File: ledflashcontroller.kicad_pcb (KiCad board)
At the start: 2 copper layers, 100 x 100 mm, 68 parts, among them J1 Conn_02x08_Odd_Even, J2 CONN_01X02, J3 CONN_01X02, K1 LDD-1000H, K2 LDD-1000H, P1 V_IN, P10 BNC, P11 BNC, P12 BNC, P2 I2C_HEADER, P3 GPIO_HEADER, P4 V_DIM1, P5 V_DIM2, P6 V_OUT, P7 BNC, P8 BNC, P9 BNC, Q1 IRLML6244, Q2 IRFB3256, U1 Teensy3.6, U10 DMC2700, U2 ISO1540, U3 DMC2700, U4 DMC2700, U5 ISO1540, U6 DMC2700, U7 DMC2700, U8 ISO1540, U9 DMC2700

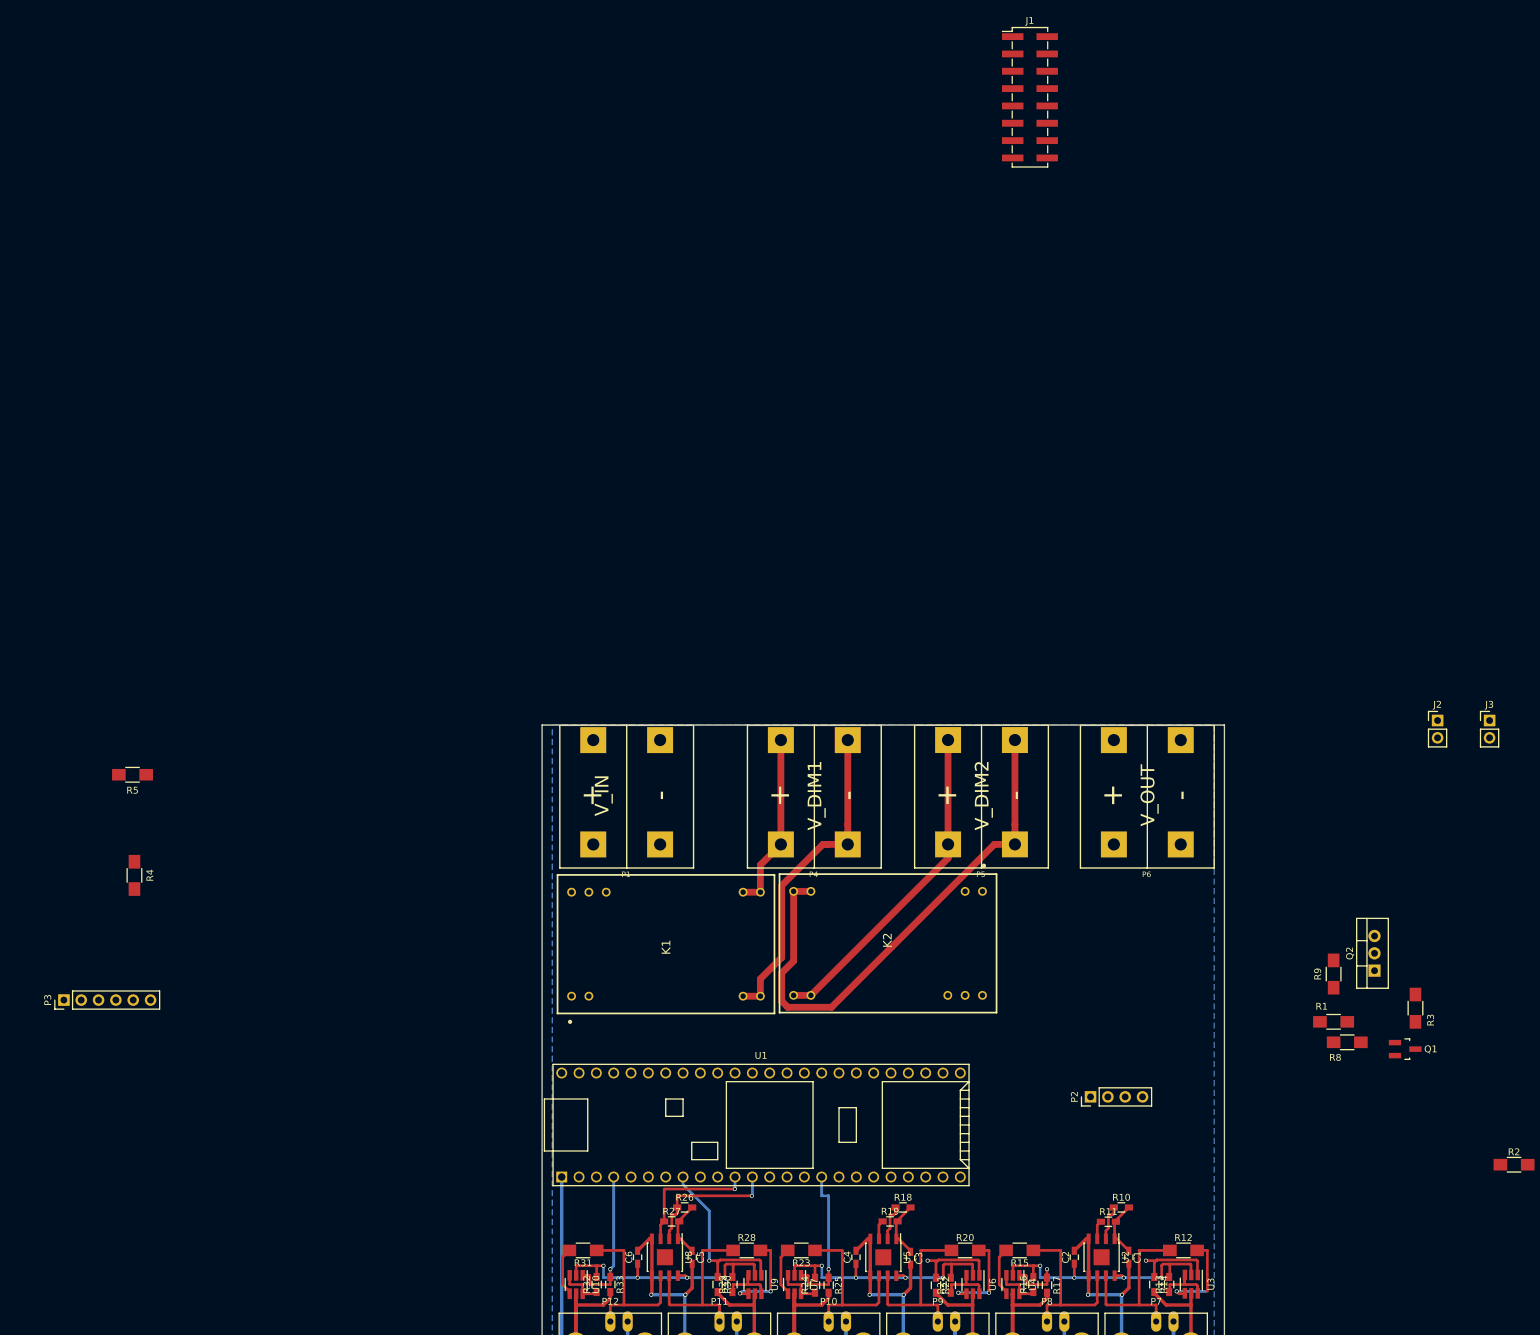
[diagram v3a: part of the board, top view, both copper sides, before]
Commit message: Fixed bugs (wires to close to pads)
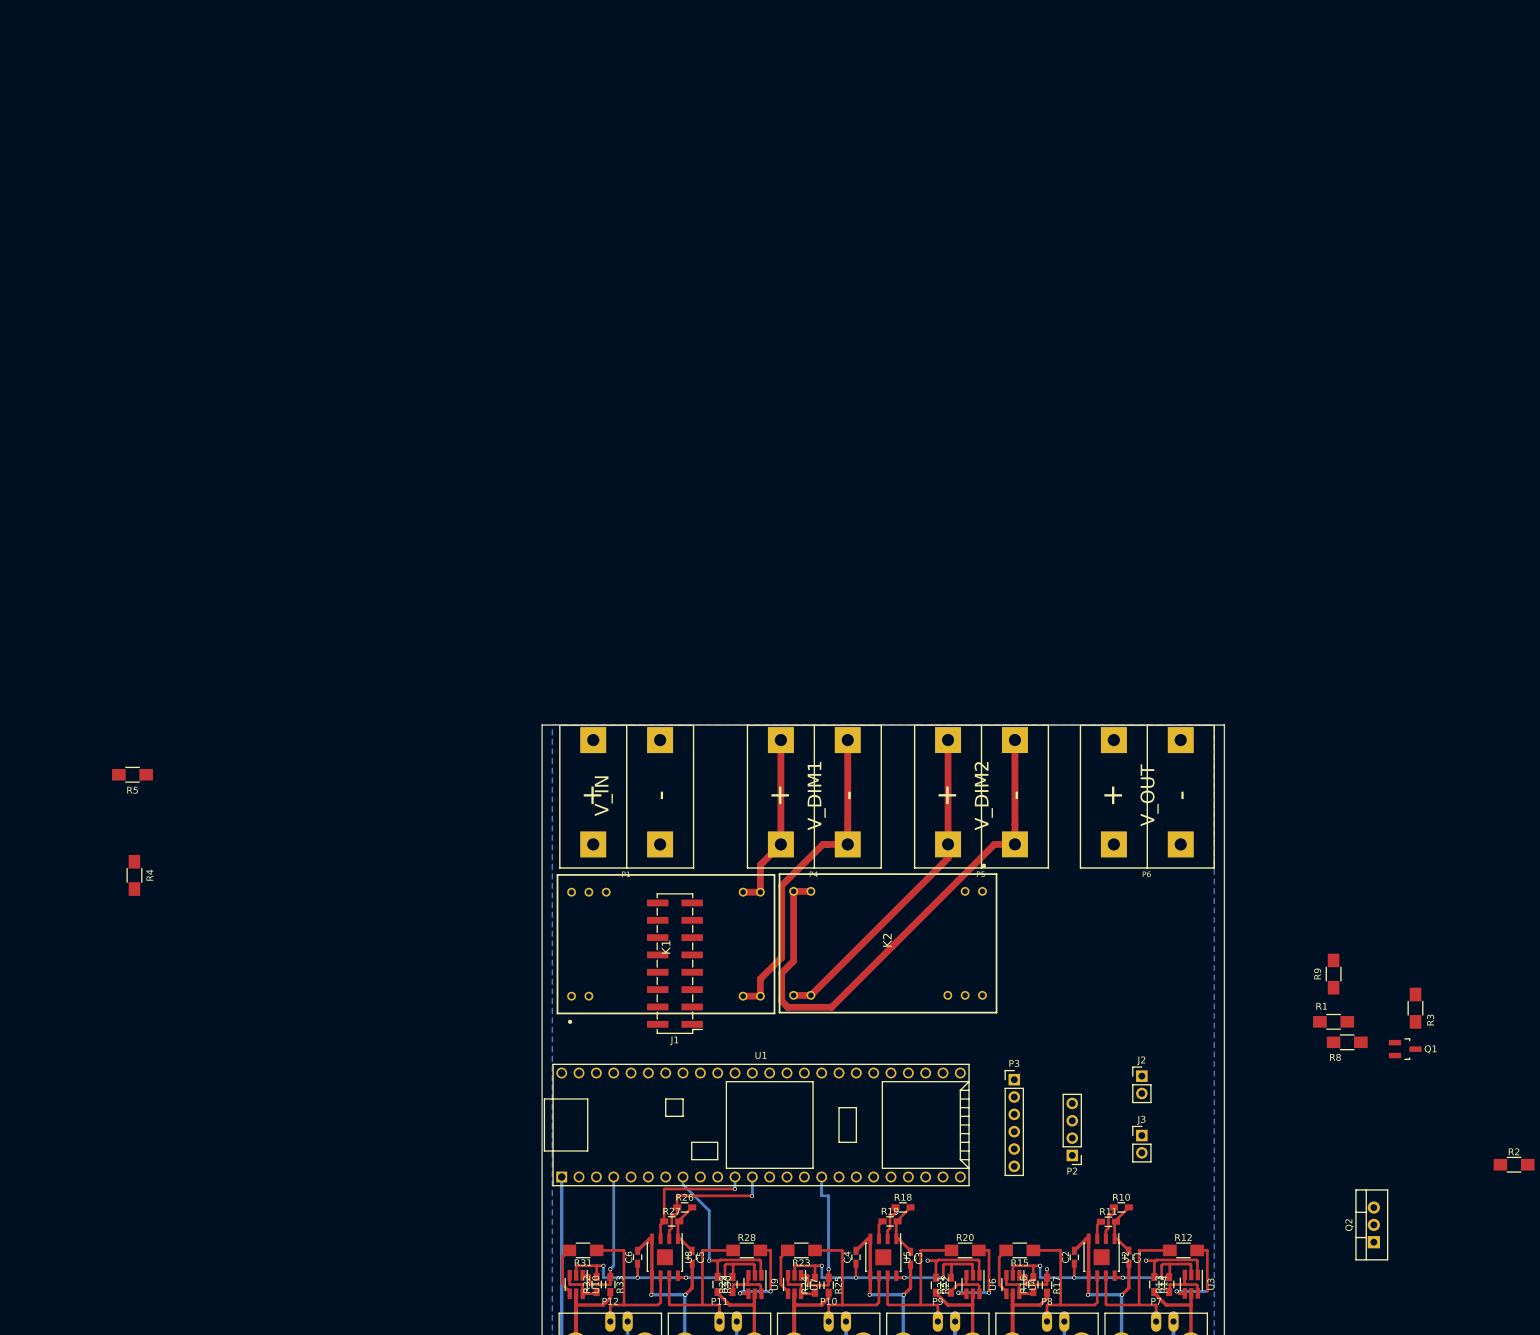
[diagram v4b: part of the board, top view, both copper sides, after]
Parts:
- moved P3 139.8 mm to (99.2, 82.0), turned to 0 degrees
- moved J1 137.2 mm to (49.5, 65.0), turned to 180 degrees
- moved J3 79.3 mm to (117.9, 90.2)
- moved J2 67.8 mm to (117.9, 81.5)
- moved Q2 39.8 mm to (151.9, 105.8)
- moved P2 8.99 mm to (107.7, 93.1), turned to 180 degrees

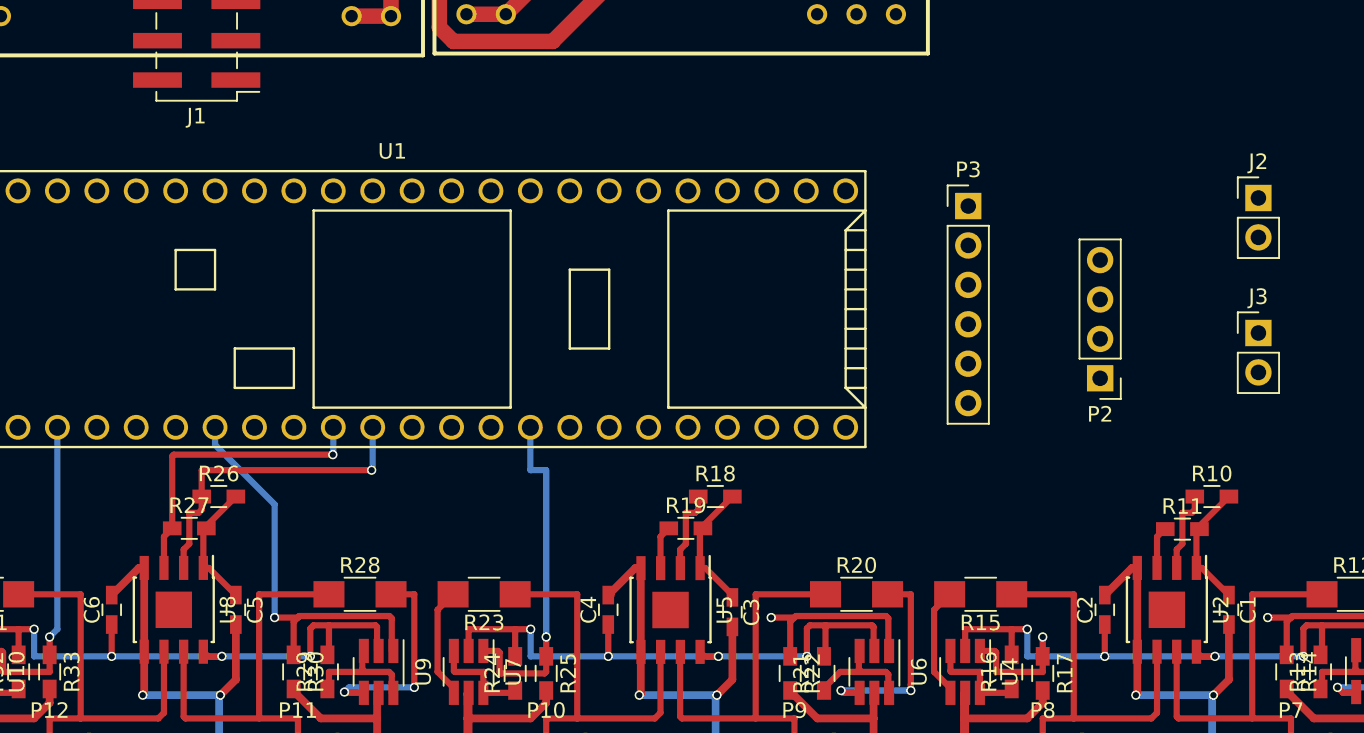
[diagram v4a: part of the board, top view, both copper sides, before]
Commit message: Connected circuits to Teensy
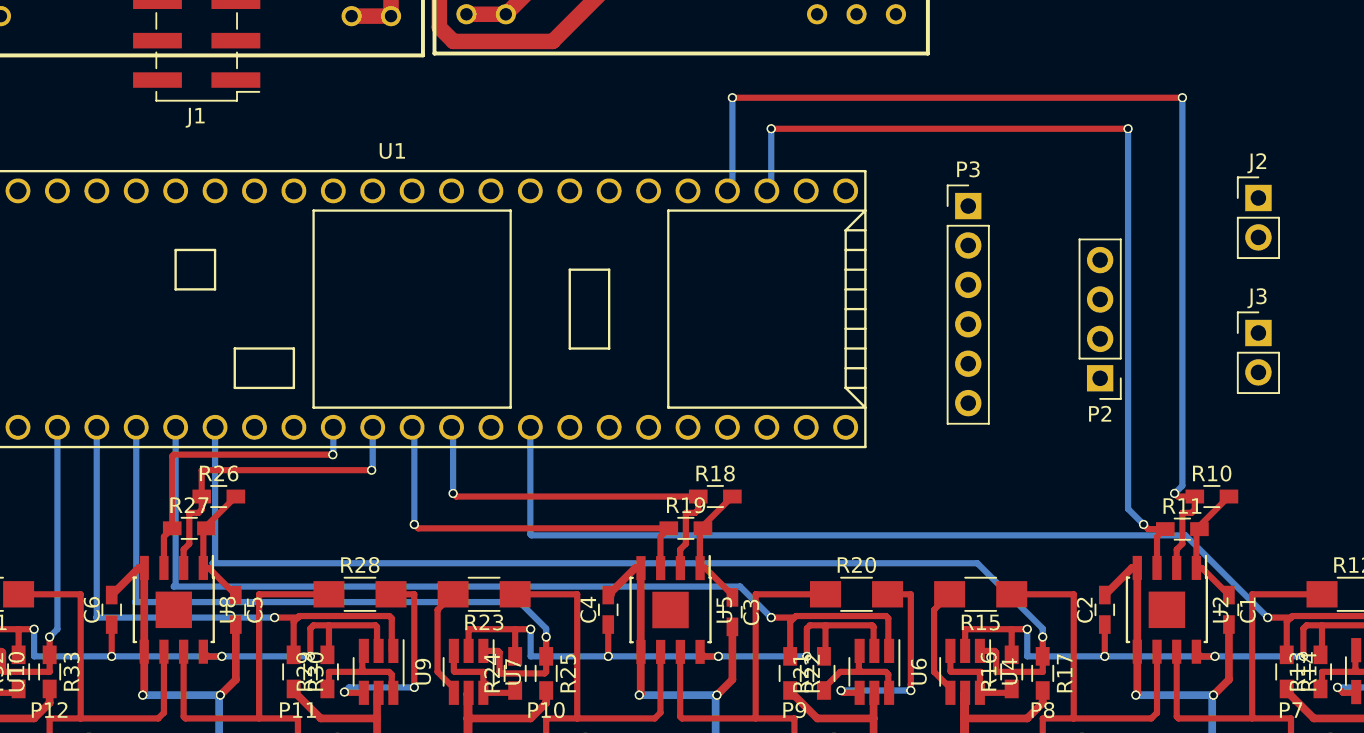
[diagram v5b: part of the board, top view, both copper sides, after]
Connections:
- R10 pad 1: /TRIG_IO0 -> /TRIG_IO9
- R11 pad 1: /TRIG_IO1 -> /TRIG_IO8
- R18 pad 1: /TRIG_IO2 -> /TRIG_IO7
- R19 pad 1: /TRIG_IO5 -> /TRIG_IO6
- U1 pad 16: /TRIG_PU5 -> /TRIG_PU0
- U1 pad 40: /TRIG_IO5 -> (no net)
- U1 pad 42: /TRIG_IO0 -> (no net)
- U1 pad 49: /TRIG_IO1 -> (no net)
- U1 pad 5: /TRIG_PU1 -> /TRIG_PU4
- U1 pad 50: /TRIG_IO2 -> (no net)
- U1 pad 6: /TRIG_PU2 -> /TRIG_PU5
- U1 pad 7: /TRIG_PU0 -> /TRIG_PU2
- U1 pad 8: /TRIG_PU4 -> /TRIG_PU1
- U2 pad 2: /TRIG_IO0 -> /TRIG_IO9
- U2 pad 3: /TRIG_IO1 -> /TRIG_IO8
- U5 pad 2: /TRIG_IO2 -> /TRIG_IO7
- U5 pad 3: /TRIG_IO5 -> /TRIG_IO6
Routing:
- net /TRIG_IO9: track 0.00 -> 67.7 mm, vias 0 -> 3
- net /TRIG_PU1: track 7.59 -> 72.2 mm
- net /TRIG_IO8: track 0.00 -> 57.3 mm, vias 0 -> 3
- net /TRIG_PU0: track 12.4 -> 69.0 mm
- net /TRIG_PU2: track 12.4 -> 62.0 mm
- net /TRIG_IO7: track 0.00 -> 25.6 mm, vias 0 -> 1
- net /TRIG_IO6: track 0.00 -> 25.6 mm, vias 0 -> 1
- net /TRIG_PU5: track 22.2 -> 46.7 mm
- net /TRIG_PU4: track 26.3 -> 36.2 mm
- net /TRIG_IO2: track 5.43 -> 0.00 mm
- net /TRIG_IO0: track 5.43 -> 0.00 mm
- net /TRIG_IO5: track 2.77 -> 0.00 mm
- net /TRIG_IO1: track 2.77 -> 0.00 mm

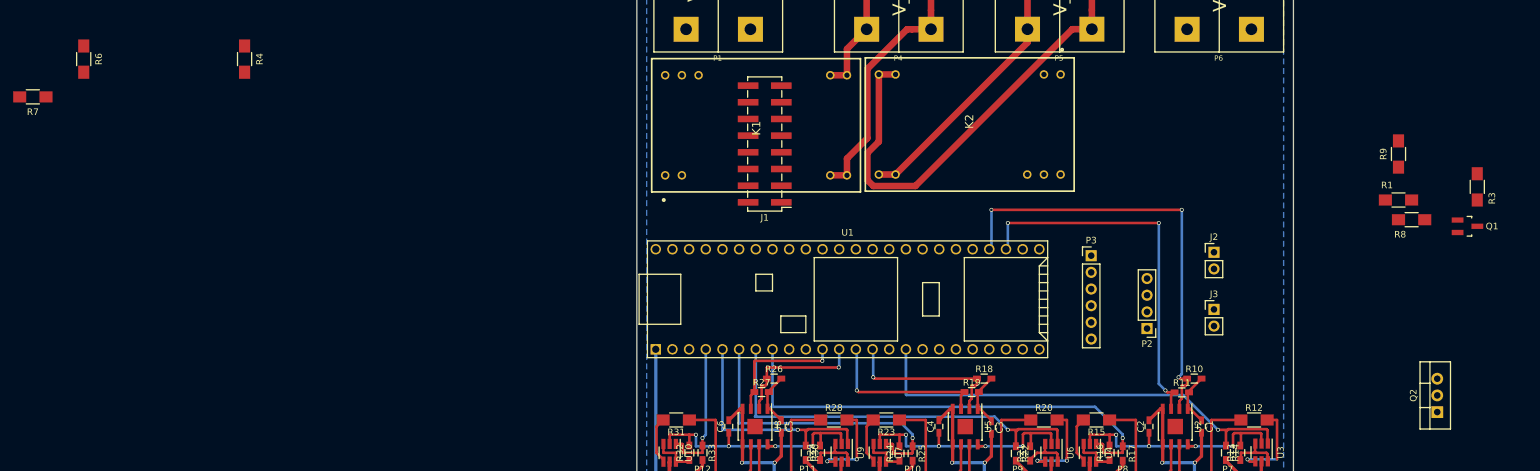
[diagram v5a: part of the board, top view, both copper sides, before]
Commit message: Changed double-usage of pins
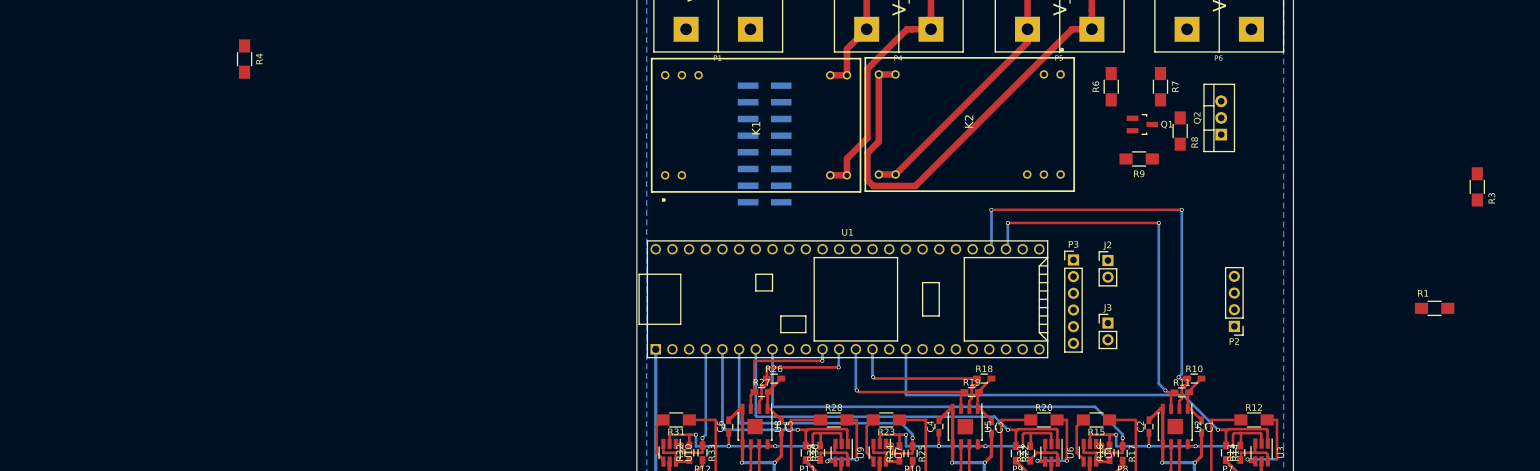
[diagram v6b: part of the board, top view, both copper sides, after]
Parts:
- J1: moved to B.Cu
- moved R7 171.7 mm to (109.8, 56.2), turned to 270 degrees
- moved R6 156.5 mm to (102.2, 56.2), turned to 90 degrees
- moved Q2 53.6 mm to (119.0, 63.5)
- moved Q1 51.9 mm to (107.0, 62.0)
- moved R9 39.5 mm to (106.5, 67.2), turned to 180 degrees
- moved R8 37.7 mm to (112.8, 63.0), turned to 90 degrees
- moved R1 17.4 mm to (151.5, 90.0)
- moved J3 16.3 mm to (101.8, 92.2)
- moved J2 16.2 mm to (101.8, 82.7)
- moved P2 13.3 mm to (121.0, 92.8)
- moved P3 2.78 mm to (96.5, 82.6)
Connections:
- J1 pad 1: /TRIG_IO6 -> /TRIG_IO0
- J1 pad 11: /TRIG_IO4 -> /TRIG_IO11
- J1 pad 3: /TRIG_IO7 -> /TRIG_IO1
- J1 pad 5: /TRIG_IO8 -> /TRIG_IO2
- J1 pad 7: /TRIG_IO9 -> /TRIG_IO5
- J1 pad 9: /TRIG_IO11 -> /TRIG_IO10
- U1 pad 34: (no net) -> /TRIG_IO10
- U1 pad 40: (no net) -> /TRIG_IO5
- U1 pad 42: (no net) -> /TRIG_IO0
- U1 pad 49: (no net) -> /TRIG_IO1
- U1 pad 50: (no net) -> /TRIG_IO2
